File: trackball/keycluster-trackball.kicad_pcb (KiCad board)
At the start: 2 copper layers, 15 x 13.4 mm, 7 parts, among them P8 CONN_7, U1 TLE4964-5M, U2 TLE4964-5M, U3 TLE4964-5M, U4 TLE4964-5M

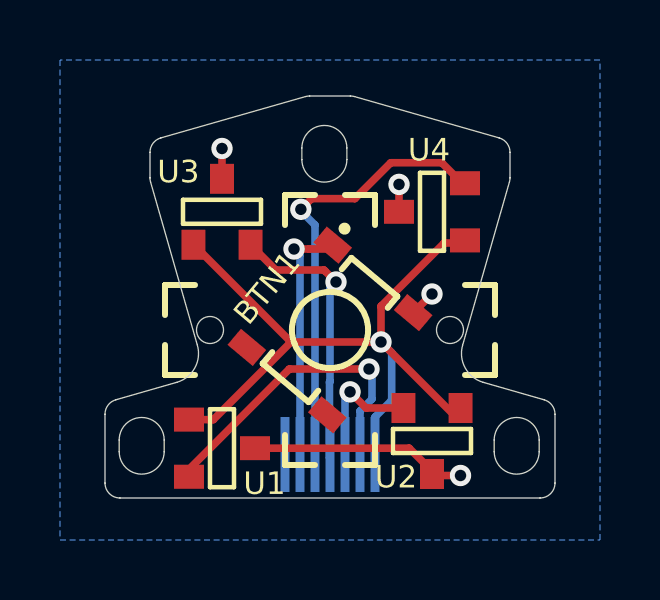
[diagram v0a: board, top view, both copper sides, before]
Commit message: Update board contour based on CAD.
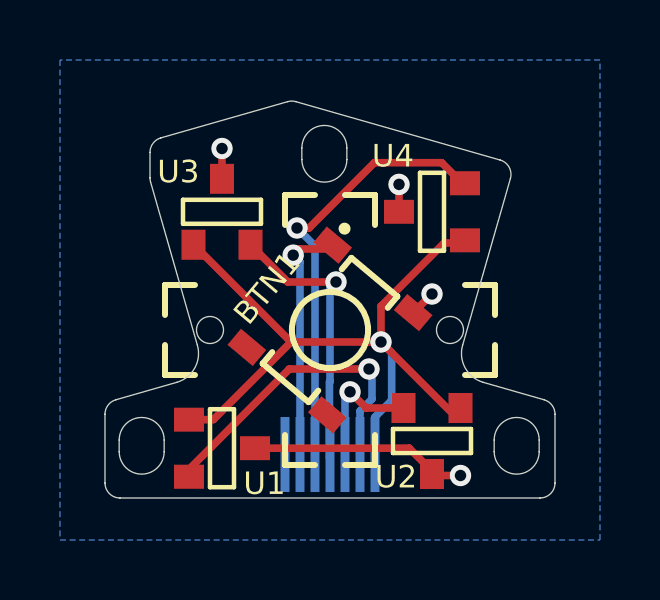
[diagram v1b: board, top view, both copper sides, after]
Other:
- board size 15 x 13.4 mm -> 15 x 13.2 mm

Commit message: Bump trackball version to 2.2.0
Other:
- board text added: "2.2.0"
- board text removed: "2.1.0"

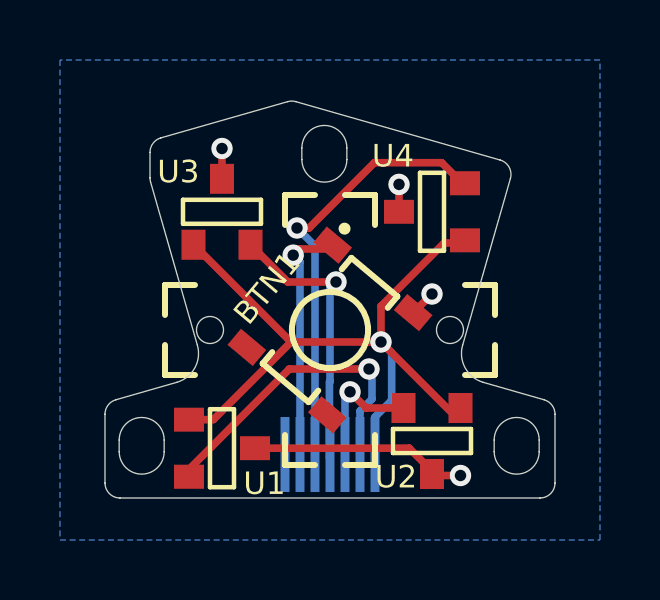
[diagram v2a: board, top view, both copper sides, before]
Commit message: Reposition FPC solder pads and bump version to 2.3.0
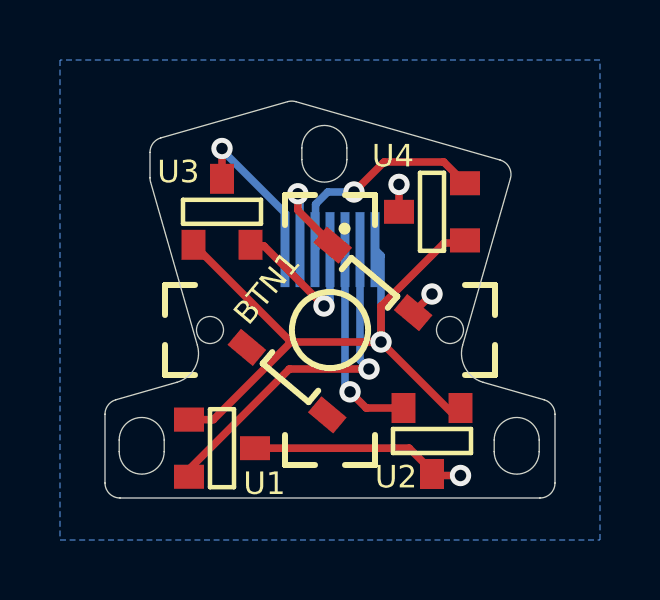
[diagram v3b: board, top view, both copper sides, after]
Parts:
- moved P8 6.83 mm to (200.0, 148.6)
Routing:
- net /TB_RIGHT: track 14.4 -> 7.69 mm
- net /TB_BTN: track 8.08 -> 3.76 mm
- net /TB_UP: track 9.33 -> 5.09 mm
- net GND: track 9.91 -> 14.1 mm
- net /TB_DOWN: track 4.29 -> 6.96 mm
- net /TB_LEFT: track 10.6 -> 12.0 mm
- net +3V3: track 24.6 -> 23.6 mm
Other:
- board text added: "2.3.0"
- board text removed: "2.2.0"
- board text removed: "PCB ID:"
